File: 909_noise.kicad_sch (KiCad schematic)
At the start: 17 parts, among them J1 Conn_01x02_Pin, J2 Conn_01x03_Pin, J3 Conn_ARM_JTAG_SWD_10, SW1 PTS645SM43SMTR92 LFS, U1 STM32G030J6Mx, U2 L78L33ABUTR, U3 TLV7211A

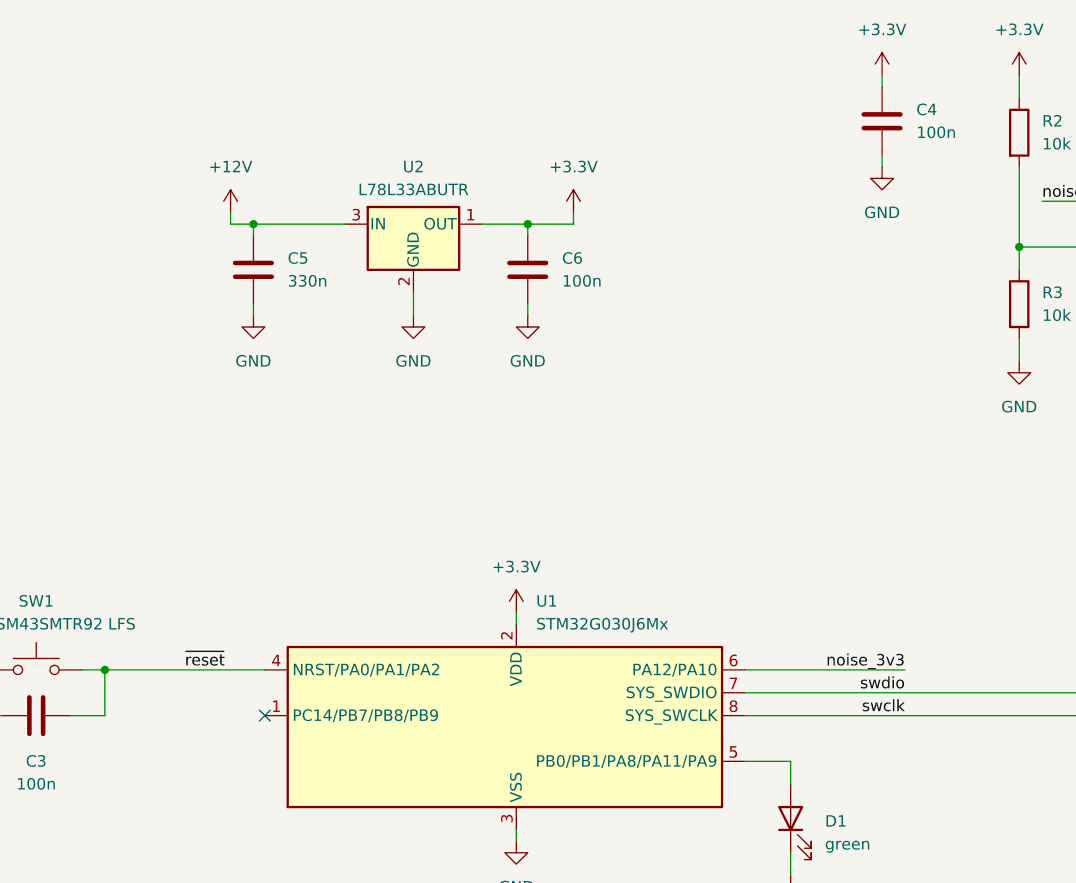
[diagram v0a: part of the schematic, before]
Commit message: initial placement, schematic tweaks
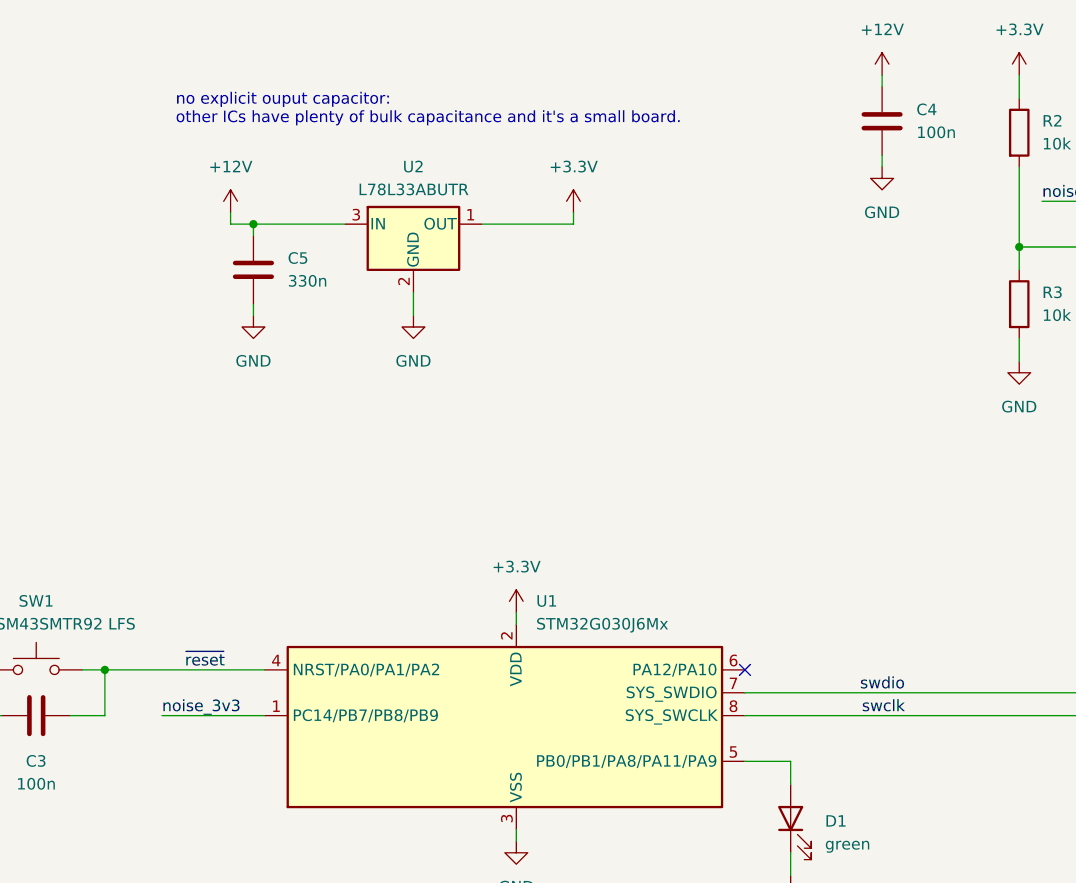
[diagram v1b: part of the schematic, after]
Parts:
- removed C6: 100n, Capacitor_SMD:C_0603_1608Metric, symbol Device:C
- J1: footprint Connector_PinHeader_2.54mm:PinHeader_1x02_P2.54mm_Vertical_SMD_Pin1Left -> Connector_PinHeader_2.54mm:PinHeader_1x02_P2.54mm_Vertical
- J2: footprint Connector_PinHeader_2.54mm:PinHeader_1x03_P2.54mm_Vertical_SMD_Pin1Left -> Connector_PinHeader_2.54mm:PinHeader_1x03_P2.54mm_Vertical
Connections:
- net +12V: now also C4.2
- net +3.3V: no longer C4.2
- net noise_3v3: now also U1.1 (PC14/PB7/PB8/PB9); no longer U1.6 (PA12/PA10)
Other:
- note added: "no explicit ouput capacitor: other ICs have plenty of bulk capacitance and it's a small board."
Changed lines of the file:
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@@
 	)
 	(junction
-		(at 135.89 38.1)
-		(diameter 0)
-		(color 0 0 0 0)
-	)
-	(junction
 		(at 105.41 38.1)
 		(diameter 0)
@@
 	)
 	(no_connect
-		(at 106.68 92.71)
+		(at 160.02 87.63)
 	)
 	(no_connect
@@
 	(wire
 		(pts
-			(xy 160.02 87.63) (xy 177.8 87.63)
-		)
-		(stroke
-			(width 0)
-			(type default)
-		)
-	)
-	(wire
-		(pts
 			(xy 175.26 30.48) (xy 175.26 31.75)
 		)
@@
 	(wire
 		(pts
-			(xy 130.81 38.1) (xy 135.89 38.1)
+			(xy 130.81 38.1) (xy 140.97 38.1)
 		)
 		(stroke
@@
 	(wire
 		(pts
-			(xy 135.89 38.1) (xy 135.89 39.37)
-		)
-		(stroke
-			(width 0)
-			(type default)
-		)
-	)
-	(wire
-		(pts
 			(xy 222.25 107.95) (xy 219.71 107.95)
 		)
@@
 	(wire
 		(pts
-			(xy 135.89 46.99) (xy 135.89 48.26)
-		)
-		(stroke
-			(width 0)
-			(type default)
-		)
-	)
-	(wire
-		(pts
 			(xy 165.1 118.11) (xy 165.1 120.65)
 		)
@@
 	(wire
 		(pts
+			(xy 95.25 92.71) (xy 106.68 92.71)
+		)
+		(stroke
+			(width 0)
+			(type default)
+		)
+	)
+	(wire
+		(pts
 			(xy 147.32 123.19) (xy 147.32 124.46)
 		)
@@
 	(wire
 		(pts
-			(xy 135.89 38.1) (xy 140.97 38.1)
-		)
-		(stroke
-			(width 0)
-			(type default)
-		)
-	)
-	(wire
-		(pts
 			(xy 72.39 87.63) (xy 72.39 92.71)
 		)
@@
 		)
 	)
+	(text "no explicit ouput capacitor: \nother ICs have plenty of bulk capacitance and it's a small board."
+		(exclude_from_sim no)
+		(at 96.774 25.4 0)
+		(effects
+			(font
+				(size 1.27 1.27)
+			)
+			(justify left)
+		)
+	)
 	(label "noise_12v"
 		(at 224.79 38.1 0)
@@
 	)
 	(label "noise_3v3"
-		(at 177.8 87.63 180)
+		(at 95.25 92.71 0)
 		(fields_autoplaced yes)
 		(effects
@@
 				(size 1.27 1.27)
 			)
-			(justify right bottom)
+			(justify left bottom)
 		)
 	)
@@
 			)
 		)
-		(property "Footprint" "Connector_PinHeader_2.54mm:PinHeader_1x03_P2.54mm_Vertical_SMD_Pin1Left"
+		(property "Footprint" "Connector_PinHeader_2.54mm:PinHeader_1x03_P2.54mm_Vertical"
 			(at 246.38 38.1 0)
 			(effects
@@
 	)
 	(symbol
-		(lib_id "Device:C")
-		(at 135.89 43.18 180)
-		(unit 1)
-		(exclude_from_sim no)
-		(in_bom yes)
-		(on_board yes)
-		(dnp no)
-		(fields_autoplaced yes)
-		(property "Reference" "C6"
-			(at 139.7 41.9099 0)
-			(effects
-				(font
-					(size 1.27 1.27)
-				)
-				(justify right)
-			)
-		)
-		(property "Value" "100n"
-			(at 139.7 44.4499 0)
-			(effects
-				(font
-					(size 1.27 1.27)
-				)
-				(justify right)
-			)
-		)
-		(property "Footprint" "Capacitor_SMD:C_0603_1608Metric"
-			(at 134.9248 39.37 0)
-			(effects
-				(font
-					(size 1.27 1.27)
-				)
-				(hide yes)
-			)
-		)
-		(property "Datasheet" "~"
-			(at 135.89 43.18 0)
-			(effects
-				(font
-					(size 1.27 1.27)
-				)
-				(hide yes)
-			)
-		)
-		(property "Description" "Unpolarized capacitor"
-			(at 135.89 43.18 0)
-			(effects
-				(font
-					(size 1.27 1.27)
-				)
-				(hide yes)
-			)
-		)
-		(pin "1"
-		)
-		(pin "2"
-		)
-		(instances
-			(project "909_noise"
-				(path "/5bcbc02e-668e-4985-8828-3c42b1486717"
-					(reference "C6")
-					(unit 1)
-				)
-			)
-		)
-	)
-	(symbol
 		(lib_id "power:PWR_FLAG")
 		(at 50.8 43.18 270)
@@
 	)
 	(symbol
-		(lib_id "power:GND")
-		(at 135.89 48.26 0)
-		(unit 1)
-		(exclude_from_sim no)
-		(in_bom yes)
-		(on_board yes)
-		(dnp no)
-		(fields_autoplaced yes)
-		(property "Reference" "#PWR022"
-			(at 135.89 54.61 0)
-			(effects
-				(font
-					(size 1.27 1.27)
-				)
-				(hide yes)
-			)
-		)
-		(property "Value" "GND"
-			(at 135.89 53.34 0)
-			(effects
-				(font
-					(size 1.27 1.27)
-				)
-			)
-		)
-		(property "Footprint" ""
-			(at 135.89 48.26 0)
-			(effects
-				(font
-					(size 1.27 1.27)
-				)
-				(hide yes)
-			)
-		)
-		(property "Datasheet" ""
-			(at 135.89 48.26 0)
-			(effects
-				(font
-					(size 1.27 1.27)
-				)
-				(hide yes)
-			)
-		)
-		(property "Description" "Power symbol creates a global label with name \"GND\" , ground"
-			(at 135.89 48.26 0)
-			(effects
-				(font
-					(size 1.27 1.27)
-				)
-				(hide yes)
-			)
-		)
-		(pin "1"
-		)
-		(instances
-			(project "909_noise"
-				(path "/5bcbc02e-668e-4985-8828-3c42b1486717"
-					(reference "#PWR022")
-					(unit 1)
-				)
-			)
-		)
-	)
-	(symbol
 		(lib_id "Comparator:MCP6561R")
 		(at 210.82 38.1 0)
@@
 	)
 	(symbol
-		(lib_id "power:+3.3V")
-		(at 175.26 21.59 0)
-		(unit 1)
-		(exclude_from_sim no)
-		(in_bom yes)
-		(on_board yes)
-		(dnp no)
-		(fields_autoplaced yes)
-		(property "Reference" "#PWR016"
-			(at 175.26 25.4 0)
-			(effects
-				(font
-					(size 1.27 1.27)
-				)
-				(hide yes)
-			)
-		)
-		(property "Value" "+3.3V"
-			(at 175.26 16.51 0)
-			(effects
-				(font
-					(size 1.27 1.27)
-				)
-			)
-		)
-		(property "Footprint" ""
-			(at 175.26 21.59 0)
-			(effects
-				(font
-					(size 1.27 1.27)
-				)
-				(hide yes)
-			)
-		)
-		(property "Datasheet" ""
-			(at 175.26 21.59 0)
-			(effects
-				(font
-					(size 1.27 1.27)
-				)
-				(hide yes)
-			)
-		)
-		(property "Description" "Power symbol creates a global label with name \"+3.3V\""
-			(at 175.26 21.59 0)
-			(effects
-				(font
-					(size 1.27 1.27)
-				)
-				(hide yes)
-			)
-		)
-		(pin "1"
-		)
-		(instances
-			(project "909_noise"
-				(path "/5bcbc02e-668e-4985-8828-3c42b1486717"
-					(reference "#PWR016")
-					(unit 1)
-				)
-			)
-		)
-	)
-	(symbol
 		(lib_id "power:GND")
 		(at 175.26 31.75 0)
@@
 			)
 		)
-		(property "Footprint" "Connector_PinHeader_2.54mm:PinHeader_1x02_P2.54mm_Vertical_SMD_Pin1Left"
+		(property "Footprint" "Connector_PinHeader_2.54mm:PinHeader_1x02_P2.54mm_Vertical"
 			(at 27.94 40.64 0)
 			(effects
@@
 					(unit 1)
 				)
+			)
+		)
+	)
+	(symbol
+		(lib_id "power:+12V")
+		(at 175.26 21.59 0)
+		(unit 1)
+		(exclude_from_sim no)
+		(in_bom yes)
+		(on_board yes)
+		(dnp no)
+		(fields_autoplaced yes)
+		(property "Reference" "#PWR016"
+			(at 175.26 25.4 0)
+			(effects
+				(font
+					(size 1.27 1.27)
+				)
+				(hide yes)
+			)
+		)
+		(property "Value" "+12V"
+			(at 175.26 16.51 0)
+			(effects
+				(font
+					(size 1.27 1.27)
+				)
+			)
+		)
+		(property "Footprint" ""
+			(at 175.26 21.59 0)
+			(effects
+				(font
+					(size 1.27 1.27)
+				)
+				(hide yes)
+			)
+		)
+		(property "Datasheet" ""
+			(at 175.26 21.59 0)
+			(effects
+				(font
+					(size 1.27 1.27)
+				)
+				(hide yes)
+			)
+		)
+		(property "Description" "Power symbol creates a global label with name \"+12V\""
+			(at 175.26 21.59 0)
+			(effects
+				(font
+					(size 1.27 1.27)
+				)
+				(hide yes)
+			)
+		)
+		(pin "1"
+		)
+		(instances
+			(project "909_noise"
+				(path "/5bcbc02e-668e-4985-8828-3c42b1486717"
+					(reference "#PWR016")
+					(unit 1)
+				)

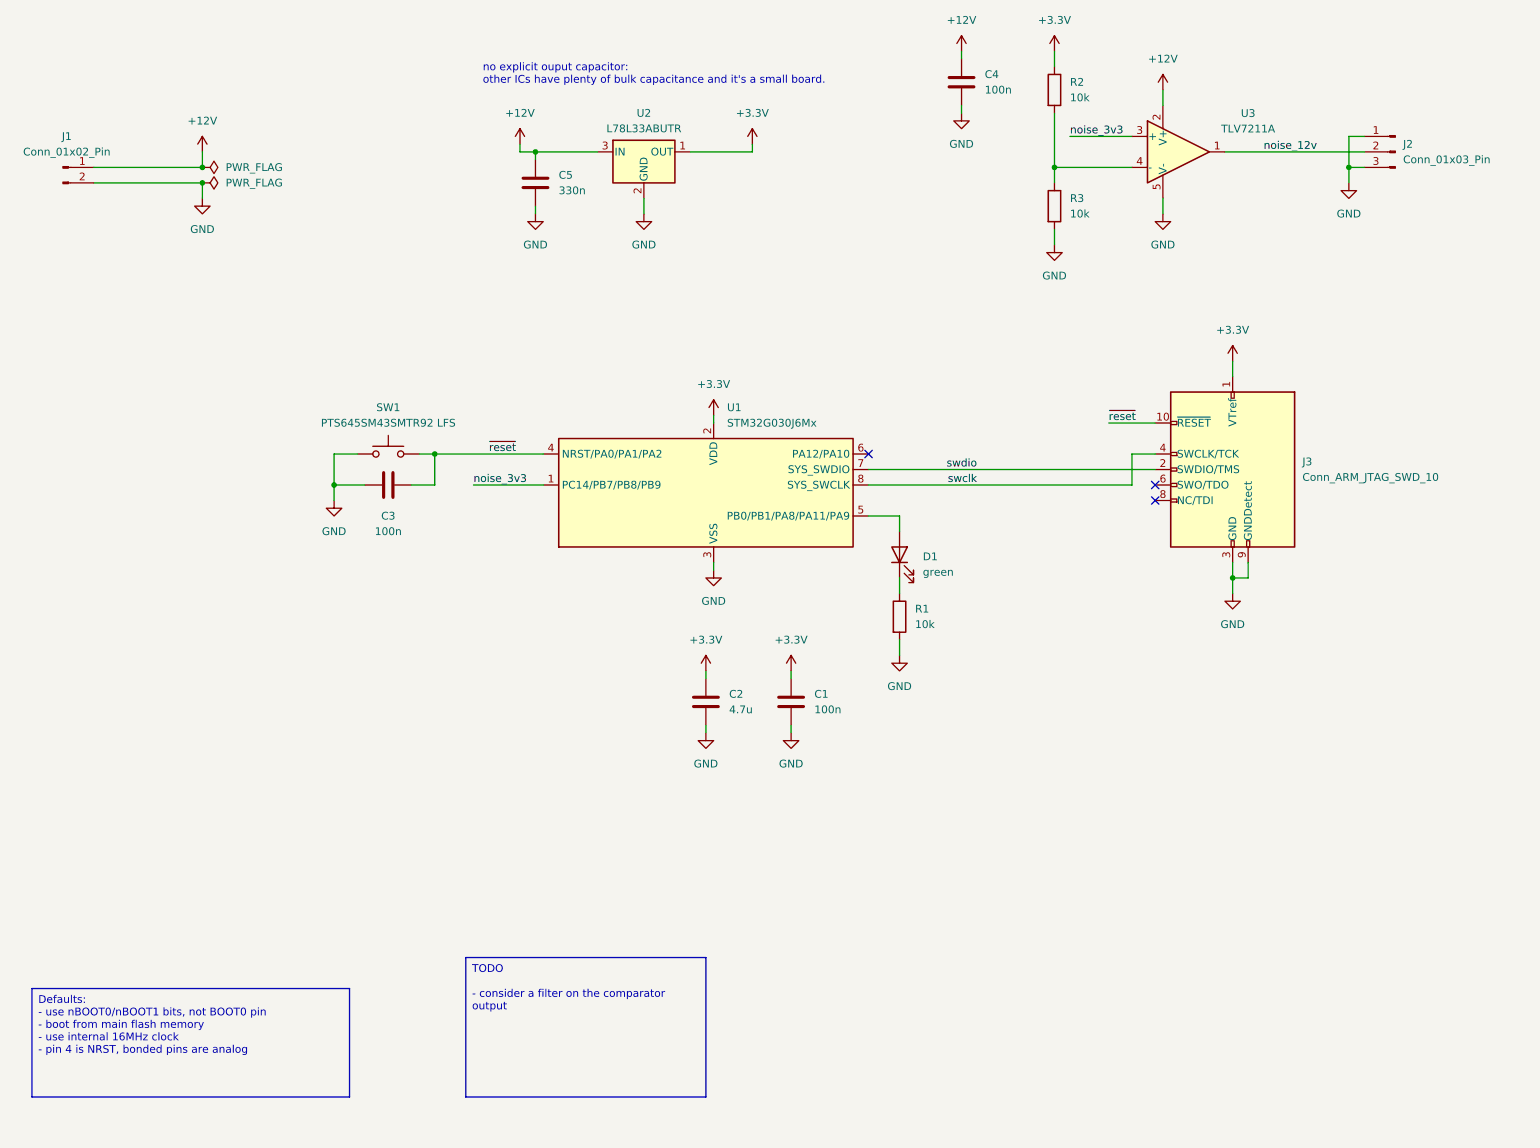
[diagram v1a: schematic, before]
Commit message: add output filter
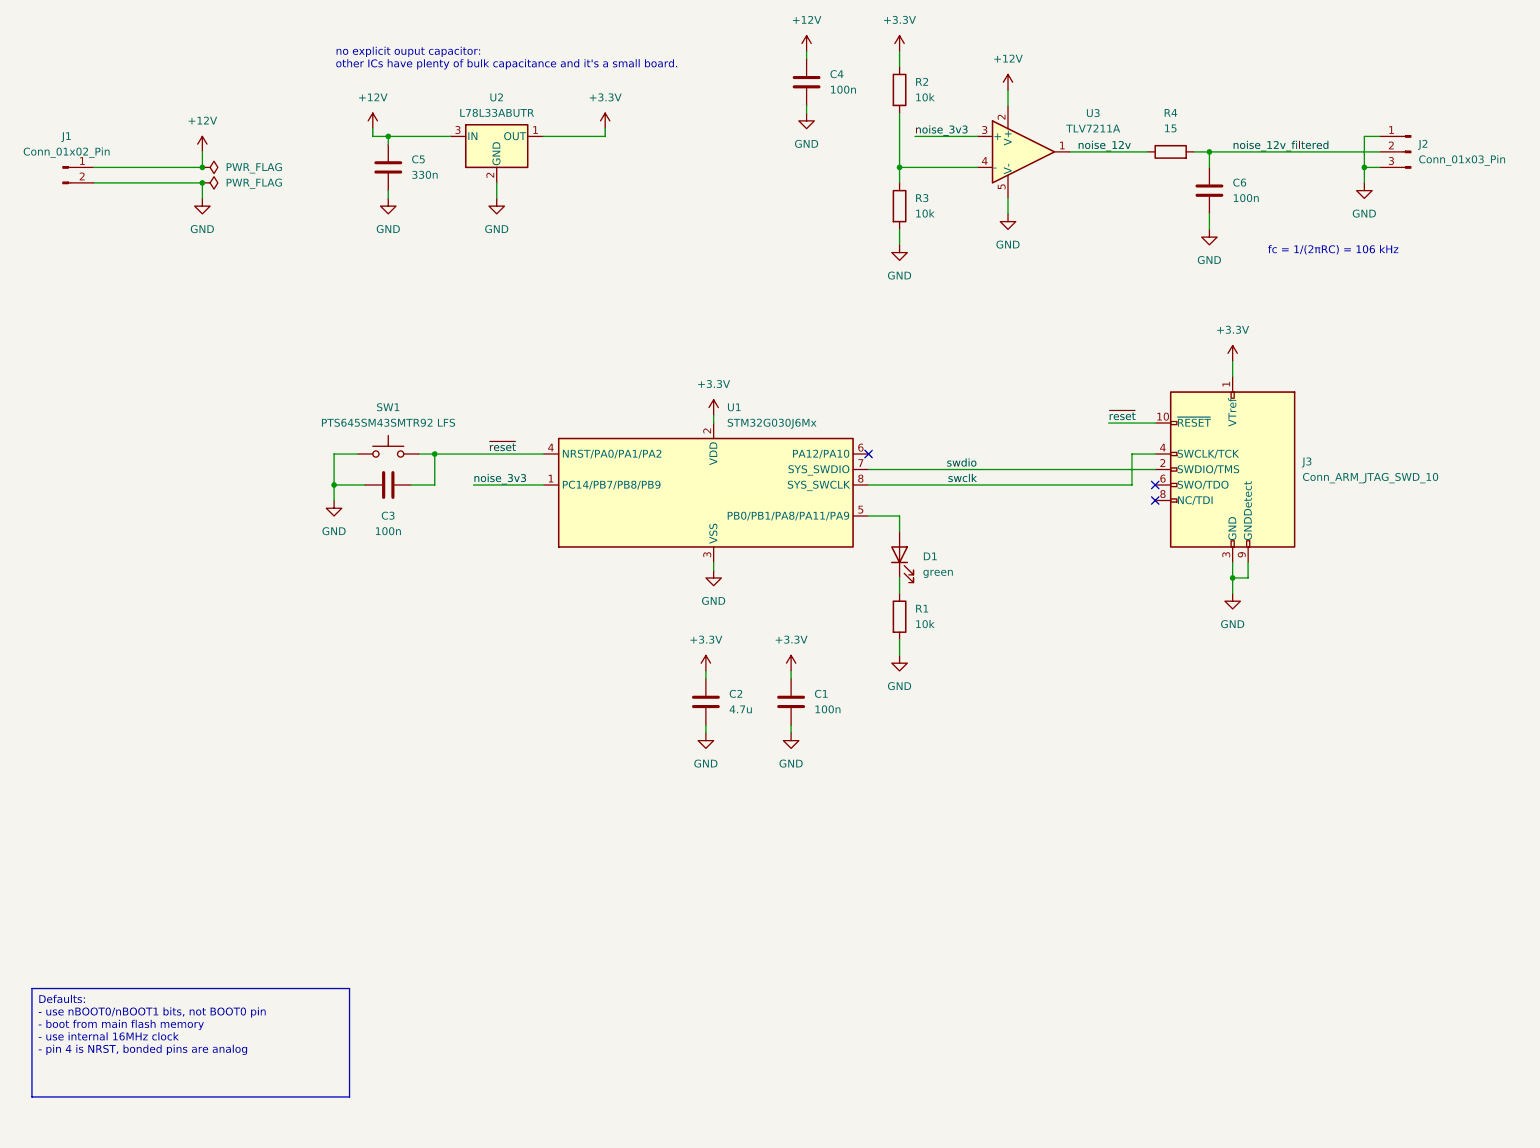
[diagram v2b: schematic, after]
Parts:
- added C6: 100n, Capacitor_SMD:C_0603_1608Metric, symbol Device:C
- added R4: 15, Resistor_SMD:R_0603_1608Metric, symbol Device:R
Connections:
- net GND: now also C6.1
- net noise_12v: now also R4.1; no longer J2.2 (Pin_2)
- new net noise_12v_filtered: C6.2, J2.2 (Pin_2), R4.2
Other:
- note added: "fc = 1/(2πRC) = 106 kHz"
- moved on the sheet: C4, C5, J2, R2, R3, U2, U3

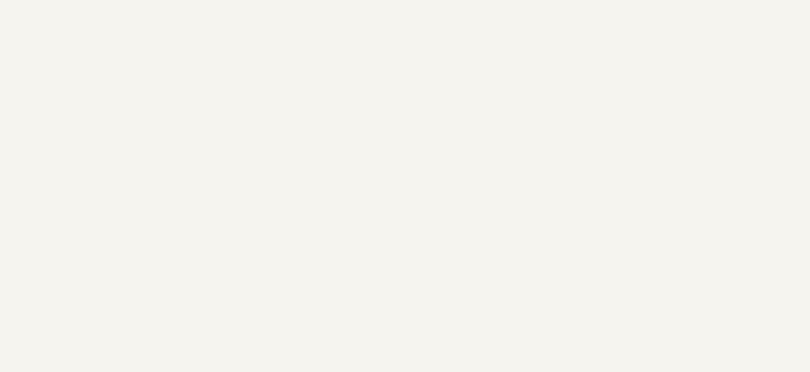
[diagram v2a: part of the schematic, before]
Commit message: add decals to back of board, rearrange silk slightly
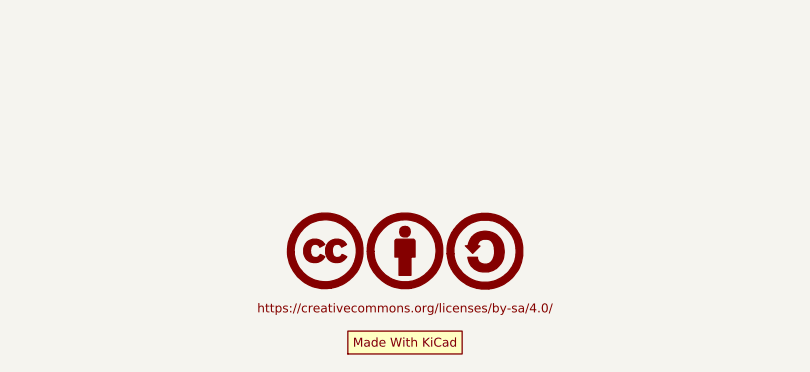
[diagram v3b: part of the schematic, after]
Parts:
- added LOGO1: CC-BY-SA_0.33in, Symbol_CreativeCommons:CC-BY-SA_SilkScreenTop_Small, symbol Creative_Commons:CC-BY-SA_0.33in
- added LOGO2: Logo_MadeWithKiCad, Symbol:KiCad-Logo2_5mm_SilkScreen, symbol Graphic_gkeeth:Logo_MadeWithKiCad
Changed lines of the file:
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@@
+	)
+	(symbol
+		(lib_id "Creative_Commons:CC-BY-SA_0.33in")
+		(at 134.62 187.96 0)
+		(unit 1)
+		(exclude_from_sim no)
+		(in_bom yes)
+		(on_board yes)
+		(dnp no)
+		(fields_autoplaced yes)
+		(property "Reference" "LOGO1"
+			(at 134.62 191.4144 0)
+			(effects
+				(font
+					(size 1.524 1.524)
+				)
+				(hide yes)
+			)
+		)
+		(property "Value" "CC-BY-SA_0.33in"
+			(at 134.62 184.5056 0)
+			(effects
+				(font
+					(size 1.524 1.524)
+				)
+				(hide yes)
+			)
+		)
+		(property "Footprint" "Symbol_CreativeCommons:CC-BY-SA_SilkScreenTop_Small"
+			(at 134.62 187.96 0)
+			(effects
+				(font
+					(size 1.27 1.27)
+				)
+				(hide yes)
+			)
+		)
+		(property "Datasheet" ""
+			(at 134.62 187.96 0)
+			(effects
+				(font
+					(size 1.27 1.27)
+				)
+				(hide yes)
+			)
+		)
+		(property "Description" ""
+			(at 134.62 187.96 0)
+			(effects
+				(font
+					(size 1.27 1.27)
+				)
+				(hide yes)
+			)
+		)
+		(instances
+			(project ""
+				(path "/5bcbc02e-668e-4985-8828-3c42b1486717"
+					(reference "LOGO1")
+					(unit 1)
+				)
+			)
+		)
 	)
 	(symbol
@@
 					(unit 1)
 				)
+			)
+		)
+	)
+	(symbol
+		(lib_id "Graphic_gkeeth:Logo_MadeWithKiCad")
+		(at 134.62 199.39 0)
+		(unit 1)
+		(exclude_from_sim no)
+		(in_bom yes)
+		(on_board yes)
+		(dnp no)
+		(fields_autoplaced yes)
+		(property "Reference" "LOGO2"
+			(at 134.62 199.39 0)
+			(effects
+				(font
+					(size 1.27 1.27)
+				)
+				(hide yes)
+			)
+		)
+		(property "Value" "Logo_MadeWithKiCad"
+			(at 134.62 199.39 0)
+			(effects
+				(font
+					(size 1.27 1.27)
+				)
+				(hide yes)
+			)
+		)
+		(property "Footprint" "Symbol:KiCad-Logo2_5mm_SilkScreen"
+			(at 134.62 199.39 0)
+			(effects
+				(font
+					(size 1.27 1.27)
+				)
+				(hide yes)
+			)
+		)
+		(property "Datasheet" ""
+			(at 134.62 199.39 0)
+			(effects
+				(font
+					(size 1.27 1.27)
+				)
+				(hide yes)
+			)
+		)
+		(property "Description" ""
+			(at 134.62 199.39 0)
+			(effects
+				(font
+					(size 1.27 1.27)
+				)
+				(hide yes)
+			)
+		)
+		(instances
+			(project ""
+				(path "/5bcbc02e-668e-4985-8828-3c42b1486717"
+					(reference "LOGO2")
+					(unit 1)
+				)
